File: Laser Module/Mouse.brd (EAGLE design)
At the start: 100 x 40 mm, 83 parts, among them Q1 MOSFET-NCHANNELAO3404A, U1 RFM69HCW, U2 HALL-EFFECTSMD, U3 HALL-EFFECTSMD, U4 HALL-EFFECTSMD, U5 HALL-EFFECTSMD, U6 BQ27441-G1, U7 BQ24075, U8 ATSAMD21G-A, U9 3.3V, Y1 32.768kHz

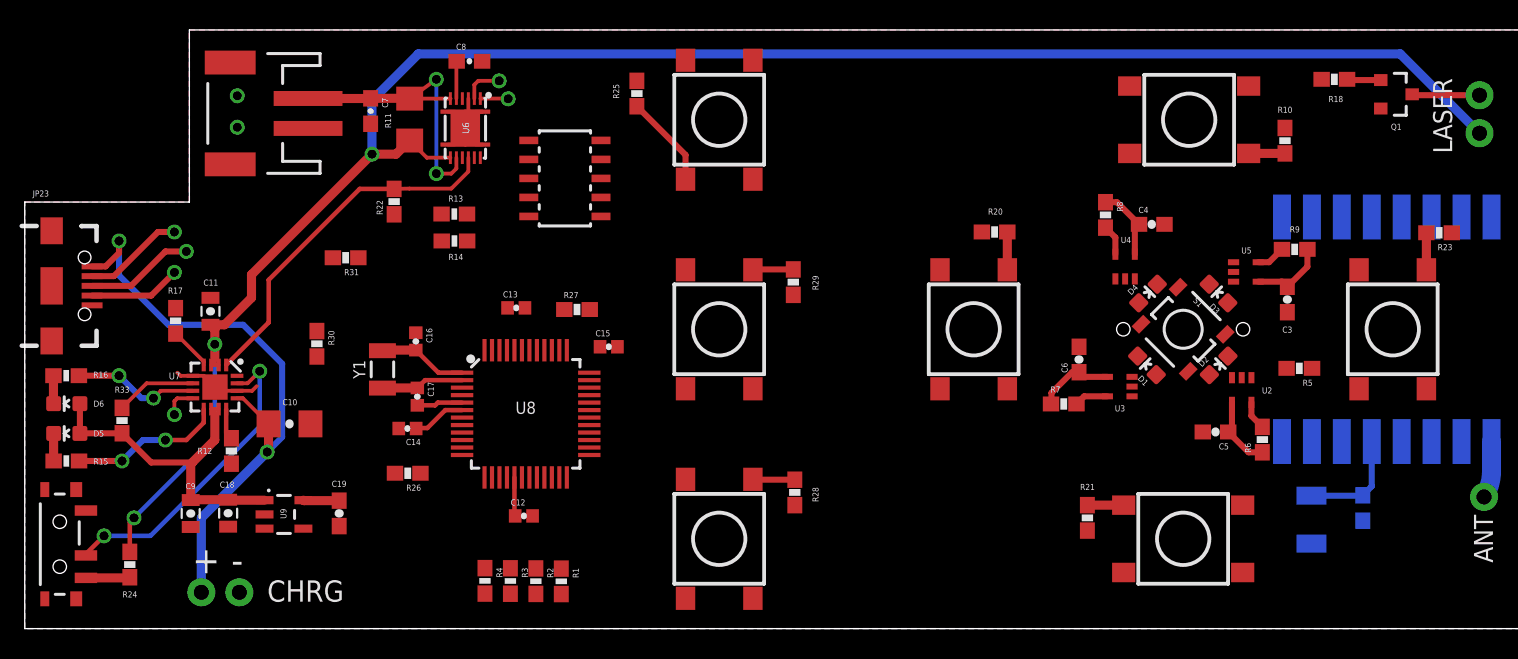
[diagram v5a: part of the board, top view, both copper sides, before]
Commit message: Finished routing the laser module
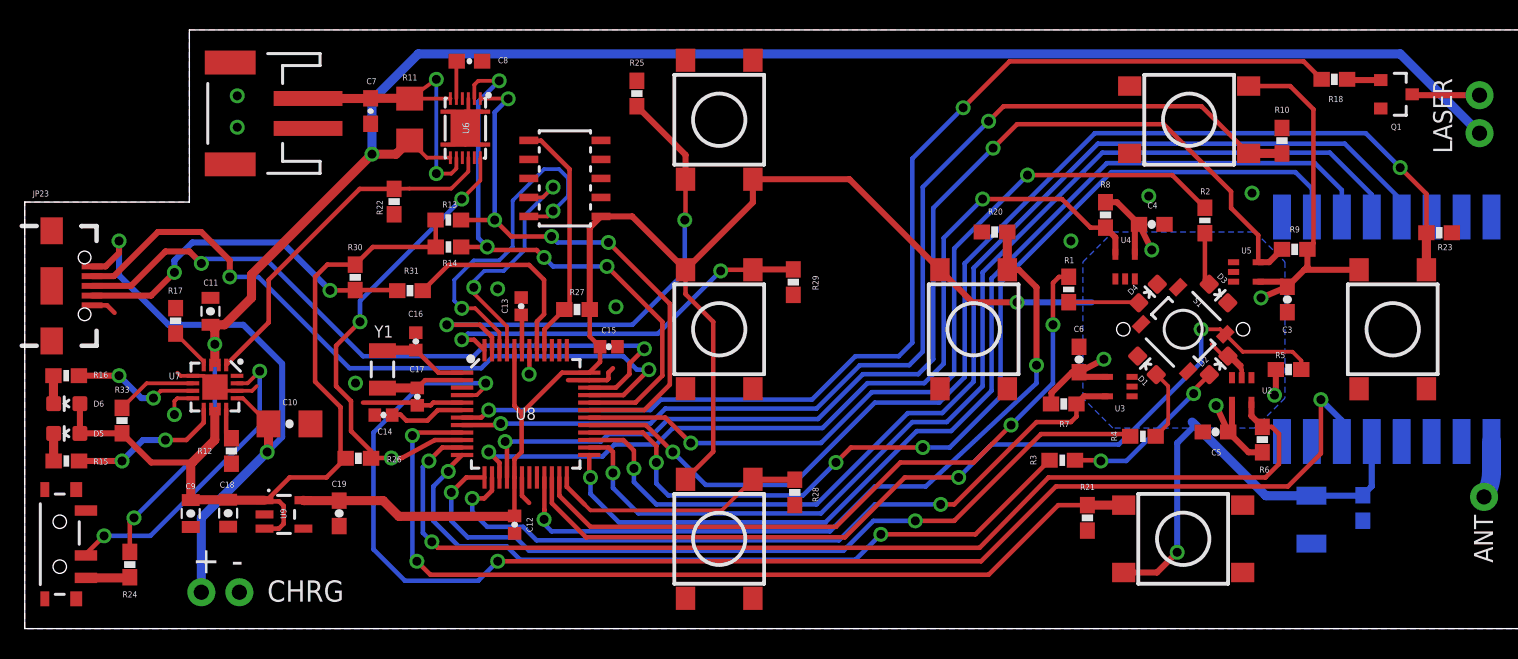
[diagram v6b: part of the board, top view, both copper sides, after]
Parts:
- moved R2 50.8 mm to (78.8, 27.3)
- moved R4 45.0 mm to (74.7, 12.8), turned to 0 degrees
- moved R1 39.1 mm to (69.8, 22.7)
- moved R3 37.7 mm to (69.3, 11.2), turned to 0 degrees
- moved R30 5.13 mm to (22.1, 23.5), turned to 90 degrees
- moved R31 4.83 mm to (25.7, 22.6)
- moved R26 3.45 mm to (22.3, 11.4)
- moved C14 1.84 mm to (24.0, 14.3)
- moved C12 0.85 mm to (32.7, 6.95), turned to 270 degrees
- moved R5 0.72 mm to (84.4, 17.3), turned to 0 degrees
- moved R14 0.57 mm to (28.3, 25.5)
- moved R13 0.57 mm to (28.3, 27.3)
- moved C13 0.35 mm to (33.2, 21.5), turned to 90 degrees
- moved R10 0.20 mm to (84.0, 32.6)
- turned D3 to 225 degrees
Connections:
- net BLU_PWM: now also U8.13; no longer U8.23
- net DWN_BTN: now also R20.2, S4.A2, U8.21; no longer R23.2, S6.A2, U8.15
- net GRN_PWM: now also U8.30; no longer U8.29
- net HALL_DWN: now also U8.14; no longer U8.47
- net HALL_LFT: now also U8.15; no longer U8.48
- net HALL_RHT: now also U8.16; no longer U8.7
- net HALL_UP: now also U8.11; no longer U8.12
- net LFT_MOUSE: now also R25.2, S7.A2, U8.47; no longer R28.2, S8.A2, U8.21
- net LSR_BTN: now also R29.2, S9.A2, U8.48; no longer R25.2, S7.A2, U8.16
- net LSR_OUT: now also U8.7; no longer U8.9
- net MDL_MOUSE: now also U8.22; no longer U8.11
- net RED_PWM: now also U8.12; no longer U8.24
- net RHT_BTN: now also U8.9; no longer U8.14
- net RHT_MOUSE: now also R28.2, S8.A2, U8.24; no longer R29.2, S9.A2, U8.22
- net UP_BTN: now also R23.2, S6.A2, U8.29; no longer R20.2, S4.A2, U8.13
- net WHT_PWM: now also U8.23; no longer U8.30
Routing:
- net 3.3V: track 32.5 -> 177.8 mm, vias 0 -> 7
- net RF_INT: track 0.00 -> 93.4 mm, vias 0 -> 3
- net UP_BTN: track 2.52 -> 78.5 mm, vias 0 -> 2
- net LSR_OUT: track 0.00 -> 75.0 mm, vias 0 -> 2
- net RF_SS: track 0.00 -> 74.4 mm, vias 0 -> 1
- net HALL_RHT: track 1.94 -> 74.9 mm, vias 0 -> 2
- net RF_SCK: track 0.00 -> 72.6 mm, vias 0 -> 1
- net HALL_UP: track 1.94 -> 73.1 mm, vias 0 -> 2
- net RF_MOSI: track 0.00 -> 70.5 mm, vias 0 -> 1
- net LFT_BTN: track 2.42 -> 71.4 mm, vias 0 -> 2
- net RF_MISO: track 0.00 -> 67.2 mm, vias 0 -> 3
- net MDL_MOUSE: track 0.00 -> 61.3 mm, vias 0 -> 2
- net RHT_BTN: track 2.42 -> 61.5 mm, vias 0 -> 2
- net HALL_LFT: track 2.05 -> 58.2 mm, vias 0 -> 2
- net GRN_PWM: track 0.00 -> 55.1 mm, vias 0 -> 2
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- added copper zone on layer 16, net 3.3V

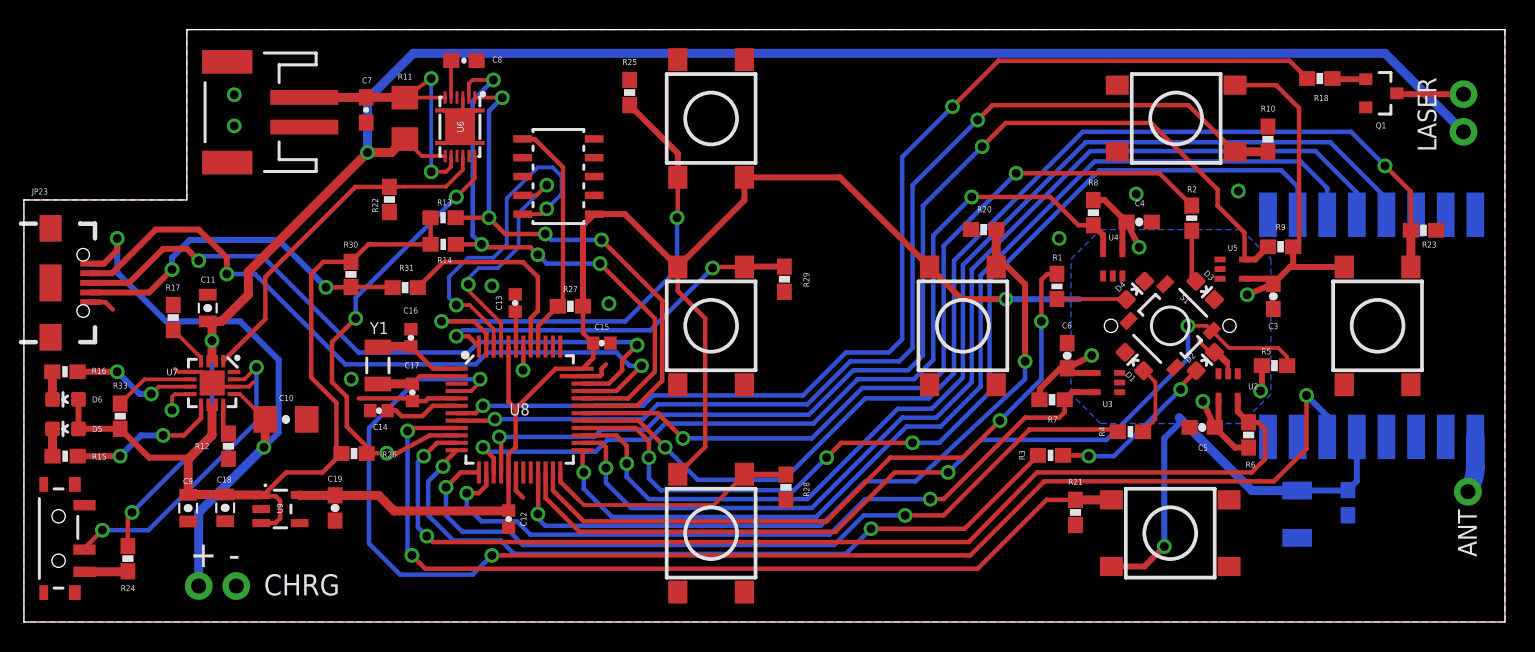
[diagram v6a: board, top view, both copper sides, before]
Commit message: Cleaned up and added text to the Laser module silkscreen
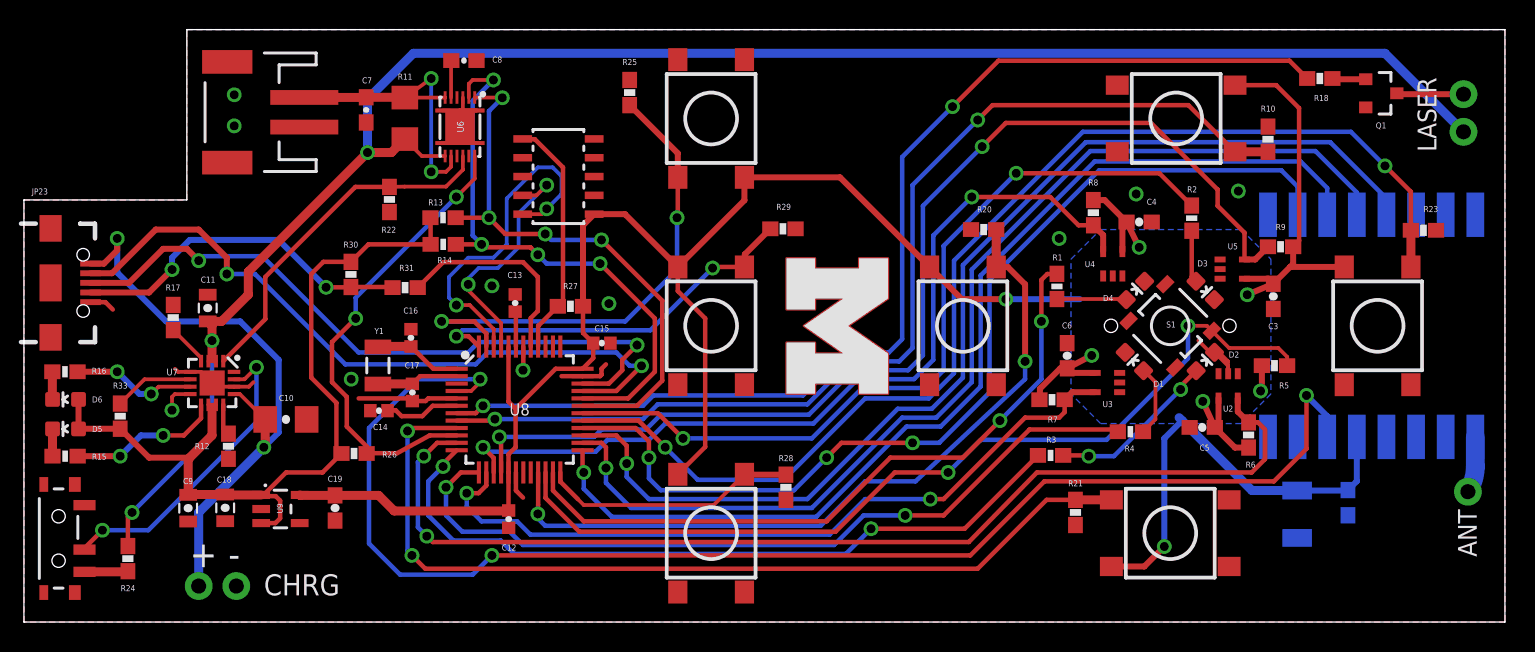
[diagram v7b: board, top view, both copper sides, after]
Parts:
- added U$2: (no value), MAAV_BlockM:BLOCK-M-10MM
- added U$3: (no value), MAAV_BlockM:BLOCK-M-10MM-MASK
- moved R29 3.40 mm to (51.2, 26.6), turned to 180 degrees
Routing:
- net LSR_BTN: track 25.9 -> 26.5 mm
- net GPOUT: vias 3 -> 2
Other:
- board text added: "AIZER"
- board text added: "Designed By: Matt Sauvé"
- board text added: "Laser Module"

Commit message: Finalized all PCBs
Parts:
- C12, C13, C14, C15: device SparkFun-Capacitors:0402-CAP -> SparkFun-Capacitors:0603-CAP
- C16, C17: device samd21-temp:0402-CAP -> SparkFun-Capacitors:0603-CAP
- C2, C3, C4, C5, C6: device SparkFun-Capacitors:0603-CAP@1 -> SparkFun-Capacitors:0603-CAP
- C7, C8: device SparkFun-Capacitors:0603-CAP@2 -> SparkFun-Capacitors:0603-CAP
- D6: value RED -> GREEN
- R1, R4: value 180 -> 91
- R16: value 1K -> 330
- R2: value 180 -> 68
- R3: value 180 -> 75
- moved JP23 0.65 mm to (1.15, 22.9)
- moved S2 0.50 mm to (2.84, 5.64)
- moved C17 0.42 mm to (26.5, 15.8)
- moved C16 0.40 mm to (26.1, 19.6)
- moved C15 0.36 mm to (38.7, 19.0)
- moved Y1 0.20 mm to (23.9, 17.5)
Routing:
- net GND: track 38.3 -> 39.5 mm, vias 10 -> 11
- net V_USB: track 40.9 -> 41.5 mm
- net USB_D-: track 48.2 -> 48.9 mm
- net N$19: track 23.7 -> 24.3 mm
- net USB_D+: track 46.5 -> 47.2 mm
- net N$5: track 2.97 -> 2.47 mm
